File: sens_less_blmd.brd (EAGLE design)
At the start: 100 x 80 mm, 7 parts

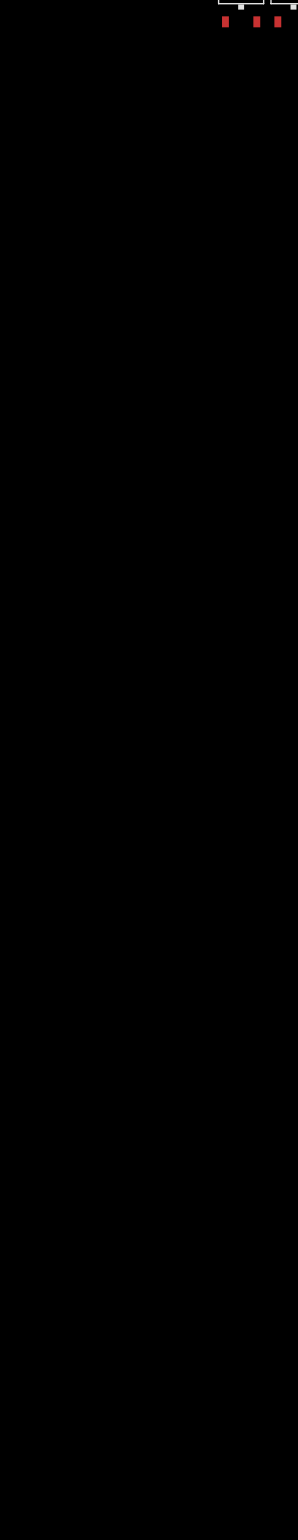
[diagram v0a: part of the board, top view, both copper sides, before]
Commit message: インバータ部を設計した
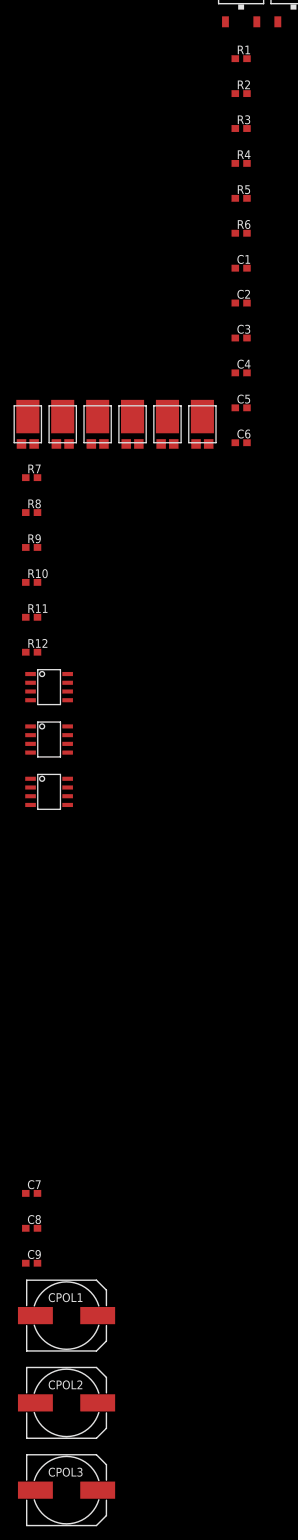
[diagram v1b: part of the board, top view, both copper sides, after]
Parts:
- added C1, C2, C3, C4, C5, C6: 4.7n, rcl:C1608
- added C7, C8, C9: 0.1u, rcl:C1608
- added CPOL1, CPOL2, CPOL3: 330u, user_rcl:1014CAPA
- added R1, R2, R3, R4, R5, R6: 10, user_rcl:1608
- added R10, R11, R12, R7, R8, R9: 10k, user_rcl:1608
- added U$10, U$11, U$12, U$13, U$8, U$9: SBR10M100P5Q, user_diode:POWERDI_5
- added U$14, U$15, U$16: ACS711, user_ic:SOIC8
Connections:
- new net GHA: R1.1, U$1.PIN11
- new net GHB: R3.1, U$1.PIN7
- new net GHC: R5.1, U$1.PIN3
- new net GLA: R2.1, U$1.PIN10
- new net GLB: R4.1, U$1.PIN6
- new net GLC: R6.1, U$1.PIN2
- new net GNDA: U$1.PAD, U$1.PAD@2
- new net MCU_GND: U$14.P$5, U$15.P$5, U$16.P$5
- new net MCU_VCC: U$14.P$8, U$15.P$8, U$16.P$8
- new net N$1: C1.1, R1.2, R7.2, U$2.PIN1
- new net N$10: C2.2, R12.1, U$14.P$1, U$14.P$2, U$3.PIN3, U$9.1, U$9.2
- new net N$12: U$14.P$3, U$14.P$4, U$15.P$3, U$15.P$4, U$16.P$3, U$16.P$4
- new net N$13: C5.2, R11.1, U$13.1, U$13.2, U$16.P$1, U$16.P$2, U$7.PIN3
- new net N$15: C4.2, R10.1, U$10.1, U$10.2, U$15.P$1, U$15.P$2, U$5.PIN3
- new net N$16: U$15.P$6
- new net N$2: C2.1, R12.2, R2.2, U$3.PIN1
- new net N$20: U$16.P$6
- new net N$3: C4.1, R10.2, R4.2, U$5.PIN1
- new net N$4: C3.1, R3.2, R9.2, U$4.PIN1
- new net N$5: C6.1, R5.2, R8.2, U$6.PIN1
- new net N$6: C5.1, R11.2, R6.2, U$7.PIN1
- new net N$9: U$14.P$6
- new net PHASE_U: C1.2, R7.1, U$2.PIN3, U$3.PIN2, U$8.1, U$8.2, U$9.3
- new net PHASE_U_I: U$14.P$7
- new net PHASE_V: C3.2, R9.1, U$10.3, U$11.1, U$11.2, U$4.PIN3, U$5.PIN2
- new net PHASE_V_I: U$15.P$7
- new net PHASE_W: C6.2, R8.1, U$12.1, U$12.2, U$13.3, U$6.PIN3, U$7.PIN2
- new net PHASE_W_I: U$16.P$7
- new net VCC: C7.1, C8.1, C9.1, CPOL1.+, CPOL2.+, CPOL3.+, U$11.3, U$12.3, U$2.PIN2, U$4.PIN2, U$6.PIN2, U$8.3
- net GND: now also C7.2, C8.2, C9.2, CPOL1.-, CPOL2.-, CPOL3.-, U$1.PIN1; no longer U$1.PAD, U$1.PAD@2

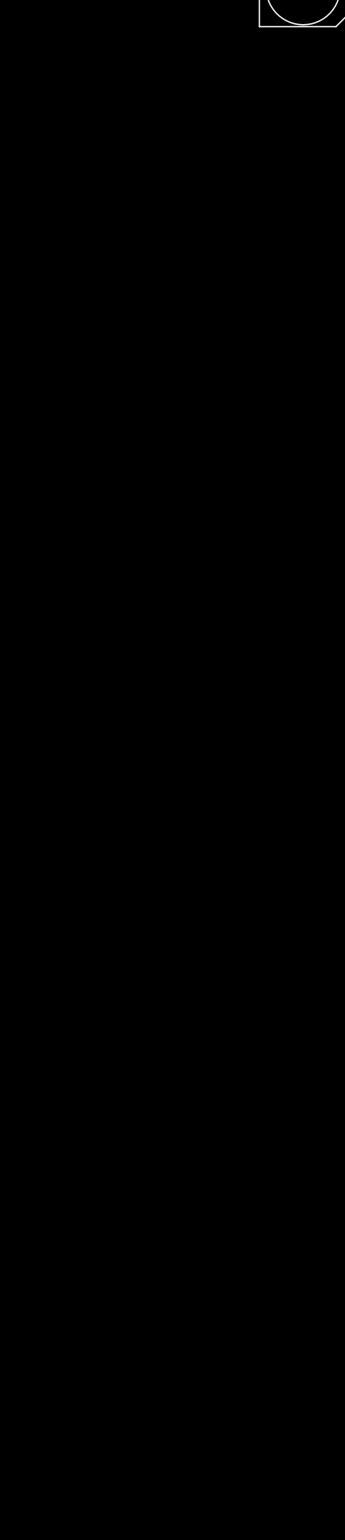
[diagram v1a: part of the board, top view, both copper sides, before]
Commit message: ドライバ側回路図の完成
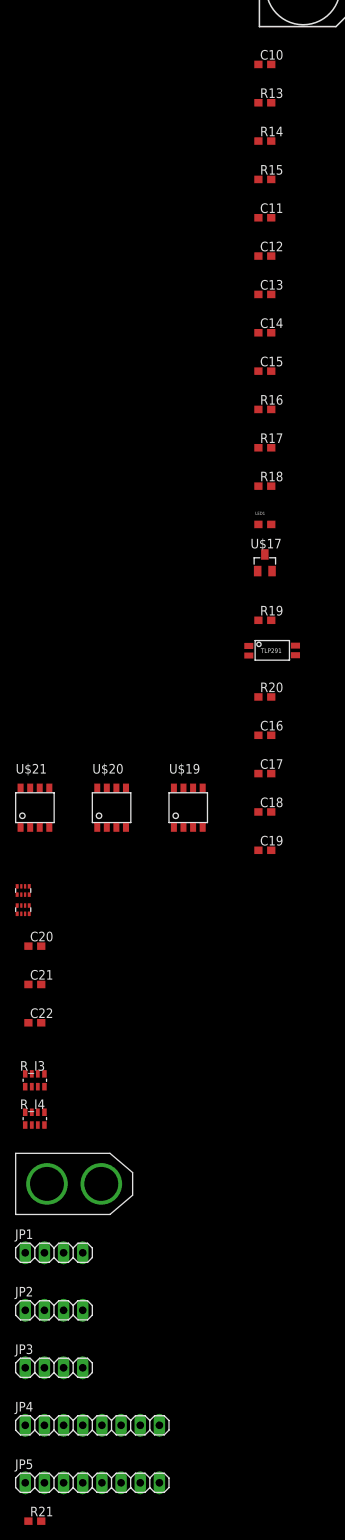
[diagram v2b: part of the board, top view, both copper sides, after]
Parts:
- added C10: 1u, rcl:C1608
- added C11, C12, C13: 0.22u, rcl:C1608
- added C14: 10u, rcl:C1608
- added C15, C17, C18, C19, C20, C21, C22: 0.1u, rcl:C1608
- added C16: (no value), rcl:C1608
- added JP1, JP2, JP3: (no value), pinhead:1X04
- added JP4, JP5: (no value), pinhead:1X08
- added LED1: (no value), user_leds:1608
- added R13, R14, R15, R18, R20: 10k, user_rcl:1608
- added R16, R17: (no value), user_rcl:1608
- added R19: 470, user_rcl:1608
- added R21: 0, user_rcl:1608
- added R_I1, R_I2: 10k, user_rcl:1005X4RESISTOR
- added R_I3, R_I4: 10k, user_rcl:0603X4RESISTOR
- added U$17: SOT23_NFET, user_tr_fet_igbt:SOT23
- added U$18: TLP291, user_ic:TLP291
- added U$19, U$20, U$21: TLP2105, user_ic:SOP8
- added U$22: XT60, user_conector:XT60
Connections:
- new net AHI: R_I2.4, U$1.PIN23, U$21.PIN6
- new net AHI_IN: JP5.3, R_I4.4
- new net ALO: R_I2.1, U$1.PIN24, U$21.PIN7
- new net ALO_IN: JP5.1, R_I4.1
- new net BHI: R_I1.4, U$1.PIN25, U$20.PIN6
- new net BHI_IN: JP4.7, R_I3.4
- new net BLO: R_I1.3, U$1.PIN26, U$20.PIN7
- new net BLO_IN: JP4.5, R_I3.3
- new net CHI: R_I1.2, U$1.PIN27, U$19.PIN6
- new net CHI_IN: JP4.3, R_I3.2
- new net CLO: R_I1.1, U$1.PIN28, U$19.PIN7
- new net CLO_IN: JP4.1, R_I3.1
- new net FAULT: R18.1, U$1.PIN22, U$17.PIN1
- new net FAULT_O: JP5.5, R20.1, U$18.PIN4
- new net N$11: LED1.K, U$17.PIN3, U$18.PIN2
- new net N$14: LED1.A, R19.1, U$18.PIN1
- new net N$17: C12.2, U$1.PIN9
- new net N$18: C11.2, U$1.PIN5
- new net N$19: R_I4.8, U$21.PIN1
- new net N$21: C19.1, C9.1, CPOL3.+, U$12.3, U$6.PIN2
- new net N$22: R_I3.5, U$20.PIN4
- new net N$23: R_I3.6, U$20.PIN1
- new net N$24: R_I3.7, U$19.PIN4
- new net N$25: R_I3.8, U$19.PIN1
- new net N$7: C10.1, U$1.PIN16
- new net N$8: C10.2, U$1.PIN15
- new net PHASE_U_FAULT: JP1.3, R13.1, U$14.P$6
- new net PHASE_V_FAULT: JP2.3, R14.1, U$15.P$6
- new net PHASE_W_FAULT: JP3.3, R15.1, U$16.P$6
- new net V5: C16.1, C20.1, C21.1, C22.1, R16.2, R18.2, R19.2, R_I1.5, R_I1.6, R_I1.7, R_I1.8, R_I2.5, R_I2.8, U$1.PIN20, U$19.PIN8, U$20.PIN8, U$21.PIN8
- new net VDSTH: R16.1, R17.2, U$1.PIN21
- net GND: now also C17.2, C19.2, R21.2, U$14.P$3, U$14.P$4, U$16.P$3, U$16.P$4, U$22.-; no longer C8.2, CPOL2.-
- net GNDA: now also C14.2, C15.2, C16.2, C20.2, C21.2, C22.2, R17.1, R21.1, U$1.PIN19, U$17.PIN2, U$19.PIN5, U$20.PIN5, U$21.PIN5
- net MCU_GND: now also JP1.4, JP2.4, JP3.4, JP4.2, JP4.4, JP4.6, JP4.8, JP5.2, JP5.4, JP5.6, U$18.PIN3, U$19.PIN2, U$19.PIN3, U$20.PIN2, U$20.PIN3, U$21.PIN2, U$21.PIN3
- net MCU_VCC: now also JP1.1, JP2.1, JP3.1, JP5.7, JP5.8, R13.2, R14.2, R15.2, R20.2
- net N$12: now also C18.2, C8.2, CPOL2.-; no longer U$14.P$3, U$14.P$4, U$16.P$3, U$16.P$4
- net N$16: now also C13.2, U$1.PIN13; no longer U$15.P$6
- net N$20: now also R_I4.5, U$21.PIN4; no longer U$16.P$6
- net N$9: now also C14.1, U$1.PIN14; no longer U$14.P$6
- net PHASE_U: now also C13.1, U$1.PIN12
- net PHASE_U_I: now also JP1.2
- net PHASE_V: now also C12.1, U$1.PIN8
- net PHASE_V_I: now also JP2.2
- net PHASE_W: now also C11.1, U$1.PIN4
- net PHASE_W_I: now also JP3.2
- net VCC: now also C15.1, C17.1, C18.1, U$1.PIN17, U$1.PIN18, U$22.+; no longer C9.1, CPOL3.+, U$12.3, U$6.PIN2

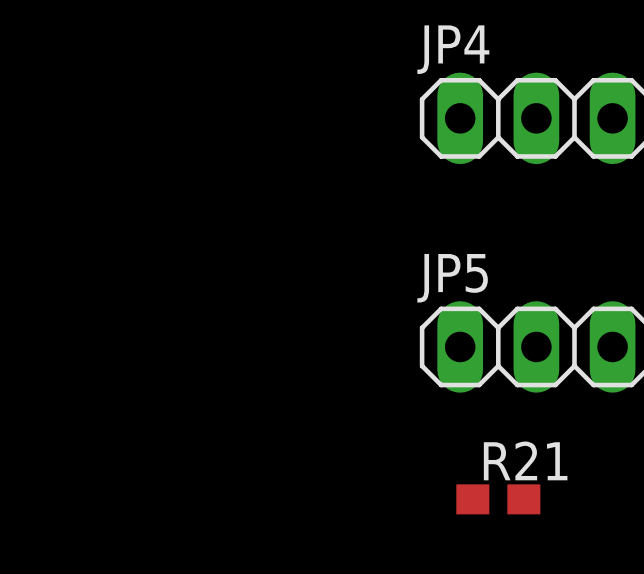
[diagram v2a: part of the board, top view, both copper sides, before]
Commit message: 電流センサの測定位置を変えた
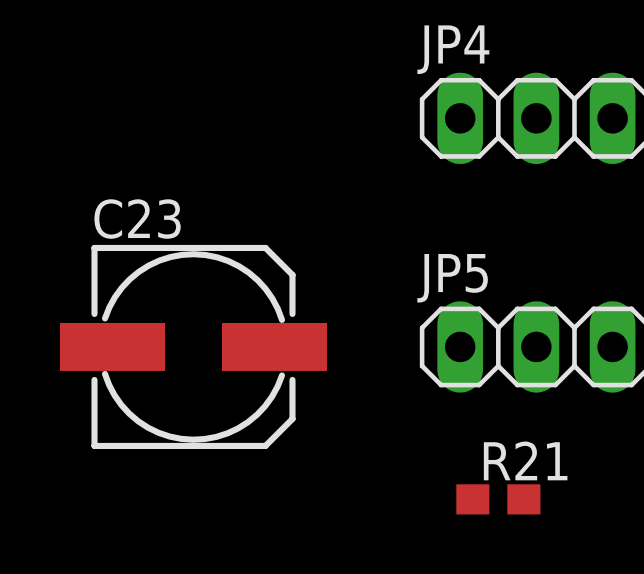
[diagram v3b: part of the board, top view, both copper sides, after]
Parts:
- added C23: 47u, rcl:153CLV-0605
- C14: value 10u -> 0.1u
- C16: value (none) -> 0.1u
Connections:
- removed net N$13: C5.2, R11.1, U$13.1, U$13.2, U$16.P$1, U$16.P$2, U$7.PIN3
- removed net N$15: C4.2, R10.1, U$10.1, U$10.2, U$15.P$1, U$15.P$2, U$5.PIN3
- new net N$26: C1.2, R7.1, U$14.P$1, U$14.P$2, U$2.PIN3, U$3.PIN2, U$8.1, U$8.2, U$9.3
- net GND: now also C18.2, C2.2, C4.2, C5.2, C8.2, CPOL2.-, R10.1, R11.1, R12.1, U$10.1, U$10.2, U$13.1, U$13.2, U$3.PIN3, U$5.PIN3, U$7.PIN3, U$9.1, U$9.2; no longer U$14.P$3, U$14.P$4, U$16.P$3, U$16.P$4
- net GNDA: now also C23.-
- net N$10: now also C6.2, R8.1, U$12.1, U$12.2, U$13.3, U$16.P$1, U$16.P$2, U$6.PIN3, U$7.PIN2; no longer C2.2, R12.1, U$14.P$1, U$14.P$2, U$3.PIN3, U$9.1, U$9.2
- net N$12: now also C3.2, R9.1, U$10.3, U$11.1, U$11.2, U$15.P$1, U$15.P$2, U$4.PIN3, U$5.PIN2; no longer C18.2, C8.2, CPOL2.-, U$15.P$3, U$15.P$4
- net N$9: now also C23.+
- net PHASE_U: now also U$14.P$3, U$14.P$4; no longer C1.2, R7.1, U$2.PIN3, U$3.PIN2, U$8.1, U$8.2, U$9.3
- net PHASE_V: now also U$15.P$3, U$15.P$4; no longer C3.2, R9.1, U$10.3, U$11.1, U$11.2, U$4.PIN3, U$5.PIN2
- net PHASE_W: now also U$16.P$3, U$16.P$4; no longer C6.2, R8.1, U$12.1, U$12.2, U$13.3, U$6.PIN3, U$7.PIN2

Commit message: 配置を大まかにきめた
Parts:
- removed C17, C18, C19, C20, C21, C22, C8, C9: 0.1u, rcl:C1608
- removed CPOL3: 330u, user_rcl:1014CAPA
- removed JP1, JP2, JP3: (no value), pinhead:1X04
- removed JP4, JP5: (no value), pinhead:1X08
- removed R14, R15, R20: 10k, user_rcl:1608
- removed R19: 470, user_rcl:1608
- removed U$16: ACS711, user_ic:SOIC8
- removed U$17: SOT23_NFET, user_tr_fet_igbt:SOT23
- removed U$18: TLP291, user_ic:TLP291
- removed U$19, U$20, U$21: TLP2105, user_ic:SOP8
- removed U$6, U$7: IPD034N06N3G, user_tr_fet_igbt:TO252
- added CON1: (no value), user_conector:XH_3P
- added CON2, CON3: (no value), user_conector:XH_4P
- added CON4: (no value), user_conector:XH_8P
- added IC_1: (no value), user_ic:TLP291
- added LED2: (no value), user_leds:1608
- added R_I5: (no value), user_rcl:0603X4RESISTOR
- added TR1, TR2, TR3, TR4, TR5, TR6: (no value), user_tr_fet_igbt:D2PACK
- C1, C2, C3, C4: value 4.7n -> 0.1u
- C5, C6: value 4.7n -> (none)
- R13, R_I4: value 10k -> (none)
- R_I1: value 10k -> (none); device user_rcl:1005X4RESISTOR -> user_rcl:0603X4RESISTOR
- R_I3: device user_rcl:0603X4RESISTOR -> user_rcl:1005X4RESISTOR
- U$2, U$3, U$4: value IPD034N06N3G -> TLP2105; device user_tr_fet_igbt:TO252 -> user_ic:SOP8
- U$5: value IPD034N06N3G -> FDC6305; device user_tr_fet_igbt:TO252 -> user_tr_fet_igbt:SSOT6
- moved C23 473.1 mm to (61.0, 30.5), turned to 180 degrees
- moved R21 448.6 mm to (55.9, 5.08), turned to 180 degrees
- moved U$22 398.7 mm to (33.0, 0.00)
- moved C16 378.3 mm to (68.6, 40.6), turned to 90 degrees
- moved R18 354.6 mm to (73.7, 45.7), turned to 270 degrees
- moved R17 345.4 mm to (73.7, 40.6), turned to 90 degrees
- moved R16 339.7 mm to (71.1, 40.6), turned to 270 degrees
- moved R_I3 333.9 mm to (-27.9, -30.5)
- moved C15 330.6 mm to (71.1, 35.6), turned to 270 degrees
- moved C14 317.0 mm to (61.0, 30.5), flipped to the bottom, turned to 180 degrees
- moved R_I1 315.5 mm to (-25.4, -25.4)
- moved C11 314.9 mm to (55.9, 45.7), turned to 270 degrees
- moved C12 314.9 mm to (55.9, 40.6), turned to 270 degrees
- moved C13 314.9 mm to (55.9, 35.6), turned to 270 degrees
- moved R_I2 314.8 mm to (-27.9, -27.9)
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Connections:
- removed net AHI_IN: JP5.3, R_I4.4
- removed net ALO_IN: JP5.1, R_I4.1
- removed net BHI_IN: JP4.7, R_I3.4
- removed net BLO_IN: JP4.5, R_I3.3
- removed net CHI_IN: JP4.3, R_I3.2
- removed net CLO_IN: JP4.1, R_I3.1
- removed net MCU_GND: JP1.4, JP2.4, JP3.4, JP4.2, JP4.4, JP4.6, JP4.8, JP5.2, JP5.4, JP5.6, U$14.P$5, U$15.P$5, U$16.P$5, U$18.PIN3, U$19.PIN2, U$19.PIN3, U$20.PIN2, U$20.PIN3, U$21.PIN2, U$21.PIN3
- removed net MCU_VCC: JP1.1, JP2.1, JP3.1, JP5.7, JP5.8, R13.2, R14.2, R15.2, R20.2, U$14.P$8, U$15.P$8, U$16.P$8
- removed net N$10: C6.2, R8.1, U$12.1, U$12.2, U$13.3, U$16.P$1, U$16.P$2, U$6.PIN3, U$7.PIN2
- removed net N$11: LED1.K, U$17.PIN3, U$18.PIN2
- removed net N$12: C3.2, R9.1, U$10.3, U$11.1, U$11.2, U$15.P$1, U$15.P$2, U$4.PIN3, U$5.PIN2
- removed net N$14: LED1.A, R19.1, U$18.PIN1
- removed net N$26: C1.2, R7.1, U$14.P$1, U$14.P$2, U$2.PIN3, U$3.PIN2, U$8.1, U$8.2, U$9.3
- removed net PHASE_U_FAULT: JP1.3, R13.1, U$14.P$6
- removed net PHASE_U_I: JP1.2, U$14.P$7
- removed net PHASE_V_FAULT: JP2.3, R14.1, U$15.P$6
- removed net PHASE_V_I: JP2.2, U$15.P$7
- removed net PHASE_W_FAULT: JP3.3, R15.1, U$16.P$6
- removed net PHASE_W_I: JP3.2, U$16.P$7
- new net AGND: LED2.K, U$5.2, U$5.5
- new net CURRENT_U: U$14.P$1, U$14.P$2
- new net CURRENT_W: U$15.P$1, U$15.P$2
- new net GNDIO: IC_1.PIN3, U$2.PIN2, U$2.PIN3, U$3.PIN2, U$3.PIN3, U$4.PIN2, U$4.PIN3
- new net IAHI: R_I5.2
- new net IALO: R_I5.1
- new net IBHI: R_I4.4
- new net IBLO: R_I4.3
- new net ICHI: R_I4.2
- new net ICLO: R_I4.1
- new net N$27: R_I4.6, U$3.PIN1
- new net N$28: R_I4.5, U$3.PIN4
- new net N$29: R_I5.8, U$4.PIN1
- new net N$30: R_I5.7, U$4.PIN4
- new net N$31: CON1.P$3
- new net N$32: CON1.P$2
- new net N$33: CON1.P$1
- new net N$34: CON2.P$4
- new net N$35: CON2.P$3
- new net N$36: CON2.P$2
- new net N$37: CON2.P$1
- new net N$38: CON3.P$4
- new net N$39: CON3.P$3
- new net N$40: CON3.P$2
- new net N$41: CON3.P$1
- new net N$42: CON4.P$8
- new net N$43: CON4.P$7
- new net N$44: CON4.P$6
- new net N$45: CON4.P$5
- new net N$46: CON4.P$4
- new net N$47: CON4.P$3
- new net N$48: CON4.P$2
- new net N$49: CON4.P$1
- new net U_GND: C5.2, U$14.P$5
- new net U_OUT: U$14.P$7
- new net U_VCC: C5.1, U$14.P$8
- new net VCCIO: R13.2
- new net W_GND: C6.2, U$15.P$5
- new net W_OUT: U$15.P$7
- new net W_VCC: C6.1, U$15.P$8
- net AHI: now also R_I2.8, U$4.PIN6; no longer R_I2.4, U$21.PIN6
- net ALO: now also R_I2.7, U$4.PIN7; no longer R_I2.1, U$21.PIN7
- net BHI: now also R_I2.6, U$3.PIN6; no longer R_I1.4, U$20.PIN6
- net BLO: now also R_I2.5, U$3.PIN7; no longer R_I1.3, U$20.PIN7
- net CHI: now also R_I3.8, U$2.PIN6; no longer R_I1.2, U$19.PIN6
- net CLO: now also R_I3.7, U$2.PIN7; no longer R_I1.1, U$19.PIN7
- net FAULT: now also U$5.1, U$5.3; no longer U$17.PIN1
- net FAULT_O: now also IC_1.PIN4, R13.1; no longer JP5.5, R20.1, U$18.PIN4
- net GND: now also C1.2, TR1.3, TR4.3, TR6.3; no longer C17.2, C18.2, C19.2, C2.2, C4.2, C5.2, C8.2, C9.2, CPOL3.-, U$3.PIN3, U$5.PIN3, U$7.PIN3
- net GNDA: now also C2.2, C3.2, C4.2, R_I2.1, R_I2.2, R_I2.3, R_I2.4, R_I3.1, R_I3.2, U$2.PIN5, U$3.PIN5, U$4.PIN5; no longer C20.2, C21.2, C22.2, U$17.PIN2, U$19.PIN5, U$20.PIN5, U$21.PIN5
- net N$1: now also TR2.1; no longer C1.1, U$2.PIN1
- net N$19: now also LED1.K, U$5.4; no longer R_I4.8, U$21.PIN1
- net N$2: now also TR1.1; no longer C2.1, U$3.PIN1
- net N$20: now also IC_1.PIN2, U$5.6; no longer R_I4.5, U$21.PIN4
- net N$21: now also IC_1.PIN1, R_I1.4; no longer C19.1, C9.1, CPOL3.+, U$12.3, U$6.PIN2
- net N$22: now also LED1.A, R_I1.3; no longer R_I3.5, U$20.PIN4
- net N$23: now also LED2.A, R_I1.1; no longer R_I3.6, U$20.PIN1
- net N$24: now also R_I4.8, U$2.PIN1; no longer R_I3.7, U$19.PIN4
- net N$25: now also R_I4.7, U$2.PIN4; no longer R_I3.8, U$19.PIN1
- net N$3: now also TR4.1; no longer C4.1, U$5.PIN1
- net N$4: now also TR3.1; no longer C3.1, U$4.PIN1
- net N$5: now also TR5.1; no longer C6.1, U$6.PIN1
- net N$6: now also TR6.1; no longer C5.1, U$7.PIN1
- net PHASE_U: now also R7.1, TR1.2, TR2.3, U$8.1, U$8.2, U$9.3
- net PHASE_V: now also R9.1, TR3.3, TR4.2, U$10.3, U$11.1, U$11.2; no longer U$15.P$3, U$15.P$4
- net PHASE_W: now also R8.1, TR5.3, TR6.2, U$12.1, U$12.2, U$13.3, U$15.P$3, U$15.P$4; no longer U$16.P$3, U$16.P$4
- net V5: now also C2.1, C3.1, C4.1, U$2.PIN8, U$3.PIN8, U$4.PIN8; no longer C20.1, C21.1, C22.1, R19.2, R_I1.7, R_I2.5, R_I2.8, U$19.PIN8, U$20.PIN8, U$21.PIN8
- net VCC: now also C1.1, TR2.2, TR3.2, TR5.2, U$12.3; no longer C17.1, C18.1, C8.1, U$2.PIN2, U$4.PIN2

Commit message: 配置を少し整えた
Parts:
- R13: value (none) -> 10k
- moved CON2 188.5 mm to (86.4, 73.7)
- moved CON3 188.5 mm to (86.4, 66.0)
- moved C6 184.9 mm to (25.4, 76.2), turned to 180 degrees
- moved CON1 164.2 mm to (99.1, 35.6), turned to 90 degrees
- moved CON4 161.1 mm to (99.1, 7.62), turned to 180 degrees
- moved R13 153.2 mm to (91.4, 48.3), turned to 90 degrees
- moved R_I5 136.8 mm to (91.4, 10.2)
- moved C2 132.9 mm to (94.0, 22.9)
- moved R_I1 131.1 mm to (86.4, 43.2), turned to 180 degrees
- moved U$5 130.6 mm to (91.4, 40.6)
- moved LED2 129.5 mm to (88.9, 48.3), turned to 90 degrees
- moved C3 128.5 mm to (86.4, 22.9)
- moved C5 126.4 mm to (22.9, 20.3), turned to 180 degrees
- moved R_I4 125.5 mm to (81.3, 10.2)
- moved LED1 125.0 mm to (86.4, 48.3), turned to 90 degrees
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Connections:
- removed net N$31: CON1.P$3
- removed net N$32: CON1.P$2
- removed net N$33: CON1.P$1
- removed net N$34: CON2.P$4
- removed net N$36: CON2.P$2
- removed net N$37: CON2.P$1
- removed net N$38: CON3.P$4
- removed net N$40: CON3.P$2
- removed net N$41: CON3.P$1
- removed net N$42: CON4.P$8
- removed net N$43: CON4.P$7
- removed net N$44: CON4.P$6
- removed net N$45: CON4.P$5
- removed net N$46: CON4.P$4
- removed net N$47: CON4.P$3
- removed net N$48: CON4.P$2
- removed net N$49: CON4.P$1
- net FAULT_O: now also CON1.P$2
- net GNDIO: now also CON1.P$1, CON4.P$1
- net IAHI: now also CON4.P$3
- net IALO: now also CON4.P$4
- net IBHI: now also CON4.P$5
- net IBLO: now also CON4.P$6
- net ICHI: now also CON4.P$7
- net ICLO: now also CON4.P$8
- net U_GND: now also CON2.P$1
- net U_OUT: now also CON2.P$2
- net U_VCC: now also CON2.P$4
- net VCCIO: now also CON1.P$3
- net W_GND: now also CON3.P$1
- net W_OUT: now also CON3.P$2
- net W_VCC: now also CON3.P$4
